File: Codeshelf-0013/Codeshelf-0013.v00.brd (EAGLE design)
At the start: 31 x 17 mm, 28 parts, among them IC1 AT45DB161D8S1

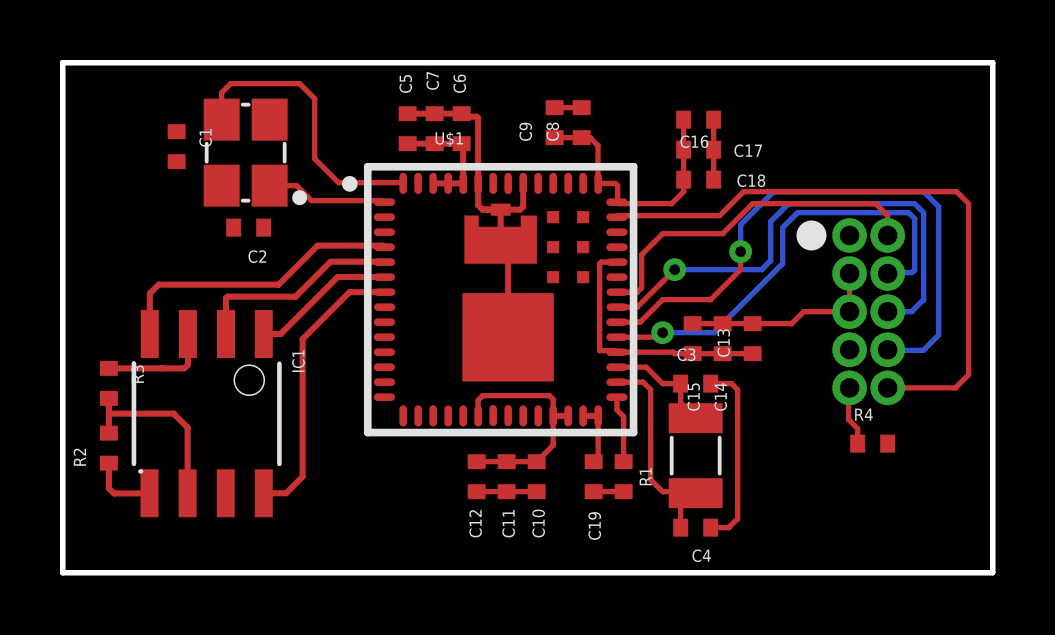
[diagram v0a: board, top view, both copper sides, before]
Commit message: KW2 and Slotflex edits
Removed RTC crystal from KW2, fixed (connected) switches in schematic of
0009.v02 and Slotflex v3 with RJ45 with NEW pinout (compatible with new
scanner pinout which doesn't exist yet in a CHE).
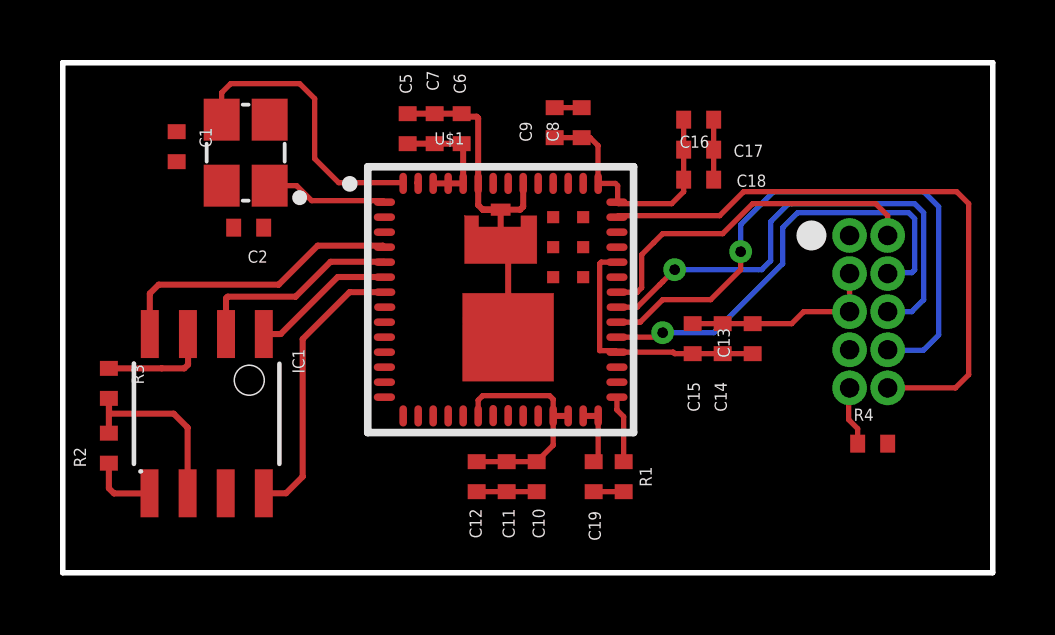
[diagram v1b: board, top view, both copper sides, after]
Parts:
- removed C3, C4: 12pF, GW-devices:C0402
- removed U$3: 32KHZ, KW2:32KHZSMD
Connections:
- removed net N$3: C4.1, U$1.P$30, U$3.P$1
- removed net N$4: C3.1, U$1.P$31, U$3.P$2
- net GND: no longer C3.2, C4.2
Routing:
- net N$3: track 7.11 -> 0.00 mm
- net GND: track 34.5 -> 28.2 mm
- net N$4: track 3.71 -> 0.00 mm
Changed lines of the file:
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@@
 <attribute name="VALUE" x="43.835" y="32.405" size="1.27" layer="27" rot="R180"/>
-</element>
-<element name="U$3" library="KW2" package="32KHZSMD" value="32KHZ" x="58.1" y="22.9" smashed="yes" rot="R270"/>
-<element name="C3" library="GW-devices" package="C0402" value="12pF" x="58.1" y="25.3" smashed="yes">
-<attribute name="NAME" x="57.465" y="26.062" size="0.4064" layer="25"/>
-<attribute name="VALUE" x="57.465" y="23.395" size="1.27" layer="27"/>
-</element>
-<element name="C4" library="GW-devices" package="C0402" value="12pF" x="58.1" y="20.5" smashed="yes">
-<attribute name="NAME" x="57.965" y="19.362" size="0.4064" layer="25"/>
-<attribute name="VALUE" x="57.465" y="18.595" size="1.27" layer="27"/>
 </element>
 <element name="C5" library="GW-devices" package="C0402" value="0.1uF" x="48.5" y="33.8" smashed="yes" rot="R90">
@@
 <contactref element="U$2" pad="P$4"/>
 <contactref element="C2" pad="2"/>
-<contactref element="C4" pad="2"/>
-<contactref element="C3" pad="2"/>
 <contactref element="C5" pad="2"/>
 <contactref element="C6" pad="2"/>
@@
 <wire x1="54.85" y1="24.225" x2="54.85" y2="22.85" width="0.1778" layer="1"/>
 <wire x1="54.85" y1="22.85" x2="54.7" y2="22.7" width="0.1778" layer="1"/>
-<wire x1="58.6" y1="25.3" x2="59.3" y2="25.3" width="0.1778" layer="1"/>
-<wire x1="59.3" y1="25.3" x2="59.5" y2="25.1" width="0.1778" layer="1"/>
-<wire x1="59.5" y1="25.1" x2="59.5" y2="20.8" width="0.1778" layer="1"/>
-<wire x1="59.5" y1="20.8" x2="59.2" y2="20.5" width="0.1778" layer="1"/>
-<wire x1="59.2" y1="20.5" x2="58.6" y2="20.5" width="0.1778" layer="1"/>
 <wire x1="58.7" y1="32.1" x2="58.7" y2="32" width="0.1778" layer="1"/>
 <wire x1="58.7" y1="32" x2="58.7" y2="33.1" width="0.1778" layer="1"/>
@@
 <vertex x="37" y="19"/>
 </polygon>
+<wire x1="54.3" y1="34.5" x2="58.7" y2="34.1" width="0" layer="19" extent="1-1"/>
+<wire x1="50.85" y1="34.15" x2="53.4" y2="34.5" width="0" layer="19" extent="1-1"/>
+<wire x1="54.35" y1="24.225" x2="51.85" y2="26.85" width="0" layer="19" extent="1-1"/>
+<wire x1="52.8" y1="21.7" x2="54.7" y2="22.7" width="0" layer="19" extent="1-1"/>
+<wire x1="58" y1="27.3" x2="54.85" y2="24.225" width="0" layer="19" extent="1-1"/>
+<wire x1="43.9" y1="34.1" x2="48.5" y2="34.3" width="0" layer="19" extent="1-1"/>
+<wire x1="42.53" y1="31.8" x2="43.81" y2="34.02" width="0" layer="19" extent="1-1"/>
+<wire x1="42.7" y1="30.5" x2="42.53" y2="31.8" width="0" layer="19" extent="1-1"/>
+<wire x1="40.8" y1="32.7" x2="42.3" y2="31.9" width="0" layer="19" extent="1-1"/>
+<wire x1="42.435" y1="21.646" x2="50.8" y2="21.7" width="0" layer="19" extent="1-1"/>
 </signal>
 <signal name="CLKM1">
@@
 <wire x1="42.3" y1="34.1" x2="40.8" y2="33.7" width="0" layer="19" extent="1-1"/>
 </signal>
-<signal name="N$3">
-<contactref element="U$3" pad="P$1"/>
-<contactref element="C4" pad="1"/>
-<contactref element="U$1" pad="P$30"/>
-<wire x1="55.475" y1="25.35" x2="56.35" y2="25.35" width="0.1778" layer="1"/>
-<wire x1="56.35" y1="25.35" x2="56.6" y2="25.1" width="0.1778" layer="1"/>
-<wire x1="56.6" y1="25.1" x2="56.6" y2="22.1" width="0.1778" layer="1"/>
-<wire x1="56.6" y1="22.1" x2="57" y2="21.7" width="0.1778" layer="1"/>
-<wire x1="57" y1="21.7" x2="57.6" y2="21.7" width="0.1778" layer="1"/>
-<wire x1="57.6" y1="21.7" x2="58.05" y2="21.7" width="0.1778" layer="1"/>
-<wire x1="58.05" y1="21.7" x2="58.1" y2="21.65" width="0.1778" layer="1"/>
-<wire x1="57.6" y1="20.5" x2="57.6" y2="21.7" width="0.1778" layer="1"/>
-</signal>
-<signal name="N$4">
-<contactref element="U$3" pad="P$2"/>
-<contactref element="C3" pad="1"/>
-<contactref element="U$1" pad="P$31"/>
-<wire x1="57.6" y1="25.3" x2="57.6" y2="24.65" width="0.1778" layer="1"/>
-<wire x1="57.6" y1="24.65" x2="58.1" y2="24.15" width="0.1778" layer="1"/>
-<wire x1="55.475" y1="25.85" x2="56.45" y2="25.85" width="0.1778" layer="1"/>
-<wire x1="56.45" y1="25.85" x2="57" y2="25.3" width="0.1778" layer="1"/>
-<wire x1="57" y1="25.3" x2="57.6" y2="25.3" width="0.1778" layer="1"/>
-</signal>
 <signal name="N$6">
